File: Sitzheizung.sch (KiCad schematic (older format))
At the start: 16 parts, among them J1 Conn_01x06_Male, Q1 BUK9M9R1-40EX, U1 TL494

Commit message: started placement
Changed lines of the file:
@@
 EESchema Schematic File Version 4
+LIBS:Sitzheizung-cache
 EELAYER 26 0
 EELAYER END
@@
 Wire Wire Line
 	1250 3450 1400 3450
-$Comp
-L power:PWR_FLAG #FLG0101
-U 1 1 5B3EE6A1
-P 5750 1600
-F 0 "#FLG0101" H 5750 1675 50  0001 C CNN
-F 1 "PWR_FLAG" H 5750 1774 50  0000 C CNN
-F 2 "" H 5750 1600 50  0001 C CNN
-F 3 "~" H 5750 1600 50  0001 C CNN
-	1    5750 1600
-	1    0    0    -1
-$EndComp
 Wire Wire Line
 	5750 1600 5750 1950
@@
 	1    0    0    -1
 $EndComp
+$Comp
+L power:PWR_FLAG #FLG0103
+U 1 1 5B3D5477
+P 5050 1600
+F 0 "#FLG0103" H 5050 1675 50  0001 C CNN
+F 1 "PWR_FLAG" H 5050 1774 50  0000 C CNN
+F 2 "" H 5050 1600 50  0001 C CNN
+F 3 "~" H 5050 1600 50  0001 C CNN
+	1    5050 1600
+	1    0    0    -1
+$EndComp
+Wire Wire Line
+	5050 1600 5050 2150
+Connection ~ 5050 2150
+$Comp
+L power:PWR_FLAG #FLG0101
+U 1 1 5B3D75B4
+P 5750 1600
+F 0 "#FLG0101" H 5750 1675 50  0001 C CNN
+F 1 "PWR_FLAG" H 5750 1774 50  0000 C CNN
+F 2 "" H 5750 1600 50  0001 C CNN
+F 3 "~" H 5750 1600 50  0001 C CNN
+	1    5750 1600
+	1    0    0    -1
+$EndComp

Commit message: finished layout
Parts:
- C1, C3: footprint Capacitors_SMD:C_0805_HandSoldering -> Capacitor_SMD:C_0805_2012Metric_Pad1.15x1.40mm_HandSolder
- C2, C4: footprint Capacitors_THT:CP_Radial_D8.0mm_P5.00mm -> Capacitor_THT:CP_Radial_D8.0mm_P5.00mm
- D1: footprint Diodes_SMD:D_MiniMELF -> Diode_SMD:D_MiniMELF
- D2: footprint LEDs:LED_0805_HandSoldering -> LED_SMD:LED_0805_2012Metric_Pad0.98x1.40mm_HandSolder
- J1: footprint (none) -> Connector_TE-Connectivity:TE_MQS_936287-2_1x06_P2.54mm_Horizontal
- R1, R2, R3, R4, R5, R6: footprint Resistors_SMD:R_0805_HandSoldering -> Resistor_SMD:R_0805_2012Metric_Pad1.15x1.40mm_HandSolder
- RV1: footprint Potentiometers:Potentiometer_Trimmer_Piher_PT-10v10_Horizontal_Px10.0mm_Py5.0mm -> Potentiometer_THT:Potentiometer_Bourns_3386X_Horizontal
- U1: footprint Housings_SOIC:SOIC-16_3.9x9.9mm_Pitch1.27mm -> Package_SO:SOIC-16_3.9x9.9mm_P1.27mm
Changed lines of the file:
@@
 F 0 "U1" H 5400 4250 50  0000 C CNN
 F 1 "TL494" H 6050 3050 50  0000 C CNN
-F 2 "Housings_SOIC:SOIC-16_3.9x9.9mm_Pitch1.27mm" H 5750 3600 50  0001 C CNN
+F 2 "Package_SO:SOIC-16_3.9x9.9mm_P1.27mm" H 5750 3600 50  0001 C CNN
 F 3 "http://www.ti.com/lit/ds/symlink/tl494.pdf" H 5750 3600 50  0001 C CNN
 	1    5750 3600
@@
 F 0 "D1" H 7650 2166 50  0000 C CNN
 F 1 "D" H 7650 2075 50  0000 C CNN
-F 2 "Diodes_SMD:D_MiniMELF" H 7650 1950 50  0001 C CNN
+F 2 "Diode_SMD:D_MiniMELF" H 7650 1950 50  0001 C CNN
 F 3 "~" H 7650 1950 50  0001 C CNN
 	1    7650 1950
@@
 F 0 "R1" H 8970 2496 50  0000 L CNN
 F 1 "650R" H 8970 2405 50  0000 L CNN
-F 2 "Resistors_SMD:R_0805_HandSoldering" V 8830 2450 50  0001 C CNN
+F 2 "Resistor_SMD:R_0805_2012Metric_Pad1.15x1.40mm_HandSolder" V 8830 2450 50  0001 C CNN
 F 3 "~" H 8900 2450 50  0001 C CNN
 	1    8900 2450
@@
 F 0 "D2" V 8938 2883 50  0000 R CNN
 F 1 "LED" V 8847 2883 50  0000 R CNN
-F 2 "LEDs:LED_0805_HandSoldering" H 8900 3000 50  0001 C CNN
+F 2 "LED_SMD:LED_0805_2012Metric_Pad0.98x1.40mm_HandSolder" H 8900 3000 50  0001 C CNN
 F 3 "~" H 8900 3000 50  0001 C CNN
 	1    8900 3000
@@
 F 0 "R5" H 7970 4296 50  0000 L CNN
 F 1 "1k8" H 7970 4205 50  0000 L CNN
-F 2 "Resistors_SMD:R_0805_HandSoldering" V 7830 4250 50  0001 C CNN
+F 2 "Resistor_SMD:R_0805_2012Metric_Pad1.15x1.40mm_HandSolder" V 7830 4250 50  0001 C CNN
 F 3 "~" H 7900 4250 50  0001 C CNN
 	1    7900 4250
@@
 F 0 "R4" V 7993 3800 50  0000 C CNN
 F 1 "15k" V 8084 3800 50  0000 C CNN
-F 2 "Resistors_SMD:R_0805_HandSoldering" V 8130 3800 50  0001 C CNN
+F 2 "Resistor_SMD:R_0805_2012Metric_Pad1.15x1.40mm_HandSolder" V 8130 3800 50  0001 C CNN
 F 3 "~" H 8200 3800 50  0001 C CNN
 	1    8200 3800
@@
 F 0 "C1" H 6765 4296 50  0000 L CNN
 F 1 "100n" H 6765 4205 50  0000 L CNN
-F 2 "Capacitors_SMD:C_0805_HandSoldering" H 6688 4100 50  0001 C CNN
+F 2 "Capacitor_SMD:C_0805_2012Metric_Pad1.15x1.40mm_HandSolder" H 6688 4100 50  0001 C CNN
 F 3 "~" H 6650 4250 50  0001 C CNN
 	1    6650 4250
@@
 F 0 "C2" H 7418 4296 50  0000 L CNN
 F 1 "10u" H 7418 4205 50  0000 L CNN
-F 2 "Capacitors_THT:CP_Radial_D8.0mm_P5.00mm" H 7338 4100 50  0001 C CNN
+F 2 "Capacitor_THT:CP_Radial_D8.0mm_P5.00mm" H 7338 4100 50  0001 C CNN
 F 3 "~" H 7300 4250 50  0001 C CNN
 	1    7300 4250
@@
 F 0 "R2" H 3520 2696 50  0000 L CNN
 F 1 "R" H 3520 2605 50  0000 L CNN
-F 2 "Resistors_SMD:R_0805_HandSoldering" V 3380 2650 50  0001 C CNN
+F 2 "Resistor_SMD:R_0805_2012Metric_Pad1.15x1.40mm_HandSolder" V 3380 2650 50  0001 C CNN
 F 3 "~" H 3450 2650 50  0001 C CNN
 	1    3450 2650
@@
 F 0 "C3" H 3565 4346 50  0000 L CNN
 F 1 "100n" H 3565 4255 50  0000 L CNN
-F 2 "Capacitors_SMD:C_0805_HandSoldering" H 3488 4150 50  0001 C CNN
+F 2 "Capacitor_SMD:C_0805_2012Metric_Pad1.15x1.40mm_HandSolder" H 3488 4150 50  0001 C CNN
 F 3 "~" H 3450 4300 50  0001 C CNN
 	1    3450 4300
@@
 F 0 "RV1" H 2680 2646 50  0000 R CNN
 F 1 "15k" H 2680 2555 50  0000 R CNN
-F 2 "Potentiometers:Potentiometer_Trimmer_Piher_PT-10v10_Horizontal_Px10.0mm_Py5.0mm" H 2750 2600 50  0001 C CNN
+F 2 "Potentiometer_THT:Potentiometer_Bourns_3386X_Horizontal" H 2750 2600 50  0001 C CNN
 F 3 "~" H 2750 2600 50  0001 C CNN
 	1    2750 2600
@@
 F 0 "C4" H 5168 4346 50  0000 L CNN
 F 1 "1u" H 5168 4255 50  0000 L CNN
-F 2 "Capacitors_THT:CP_Radial_D8.0mm_P5.00mm" H 5088 4150 50  0001 C CNN
+F 2 "Capacitor_THT:CP_Radial_D8.0mm_P5.00mm" H 5088 4150 50  0001 C CNN
 F 3 "~" H 5050 4300 50  0001 C CNN
 	1    5050 4300
@@
 F 0 "R6" H 4520 4346 50  0000 L CNN
 F 1 "1k" H 4520 4255 50  0000 L CNN
-F 2 "Resistors_SMD:R_0805_HandSoldering" V 4380 4300 50  0001 C CNN
+F 2 "Resistor_SMD:R_0805_2012Metric_Pad1.15x1.40mm_HandSolder" V 4380 4300 50  0001 C CNN
 F 3 "~" H 4450 4300 50  0001 C CNN
 	1    4450 4300
@@
 F 0 "R3" V 4700 3500 50  0000 C CNN
 F 1 "1k" V 4500 3500 50  0000 C CNN
-F 2 "Resistors_SMD:R_0805_HandSoldering" V 4530 3500 50  0001 C CNN
+F 2 "Resistor_SMD:R_0805_2012Metric_Pad1.15x1.40mm_HandSolder" V 4530 3500 50  0001 C CNN
 F 3 "~" H 4600 3500 50  0001 C CNN
 	1    4600 3500
@@
 F 0 "J1" H 1150 3550 50  0000 C CNN
 F 1 "Conn_01x06_Male" H 1150 2850 50  0000 C CNN
-F 2 "" H 1050 3250 50  0001 C CNN
+F 2 "Connector_TE-Connectivity:TE_MQS_936287-2_1x06_P2.54mm_Horizontal" H 1050 3250 50  0001 C CNN
 F 3 "~" H 1050 3250 50  0001 C CNN
 	1    1050 3250

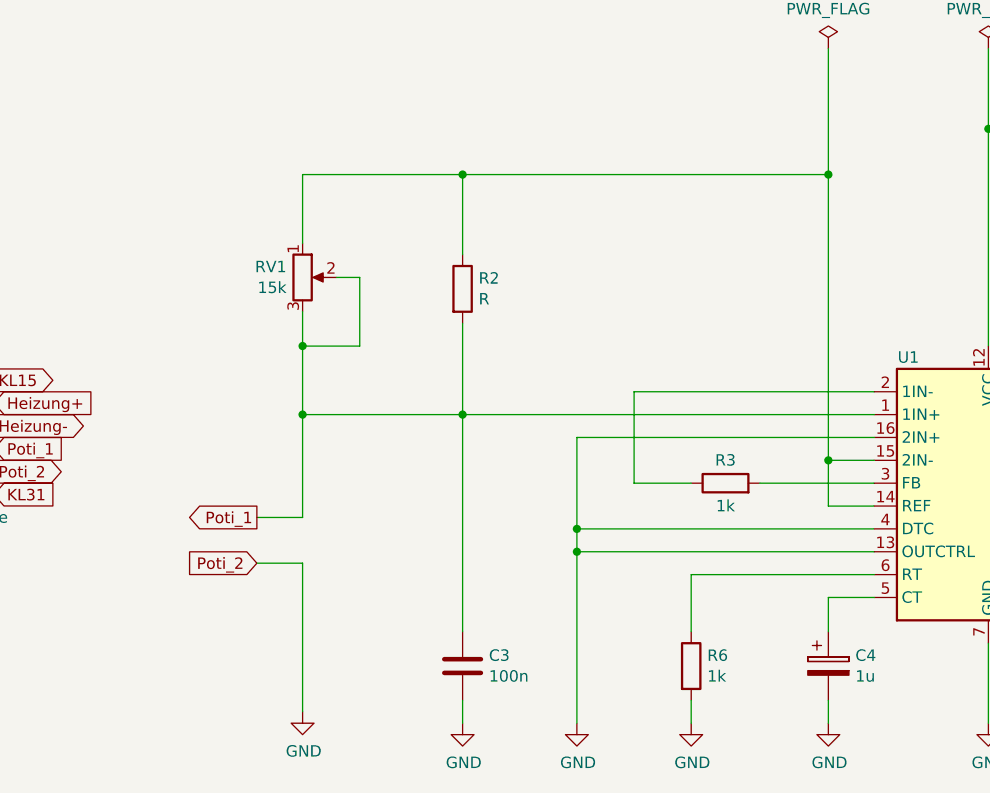
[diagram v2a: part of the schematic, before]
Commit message: changed potentiometer
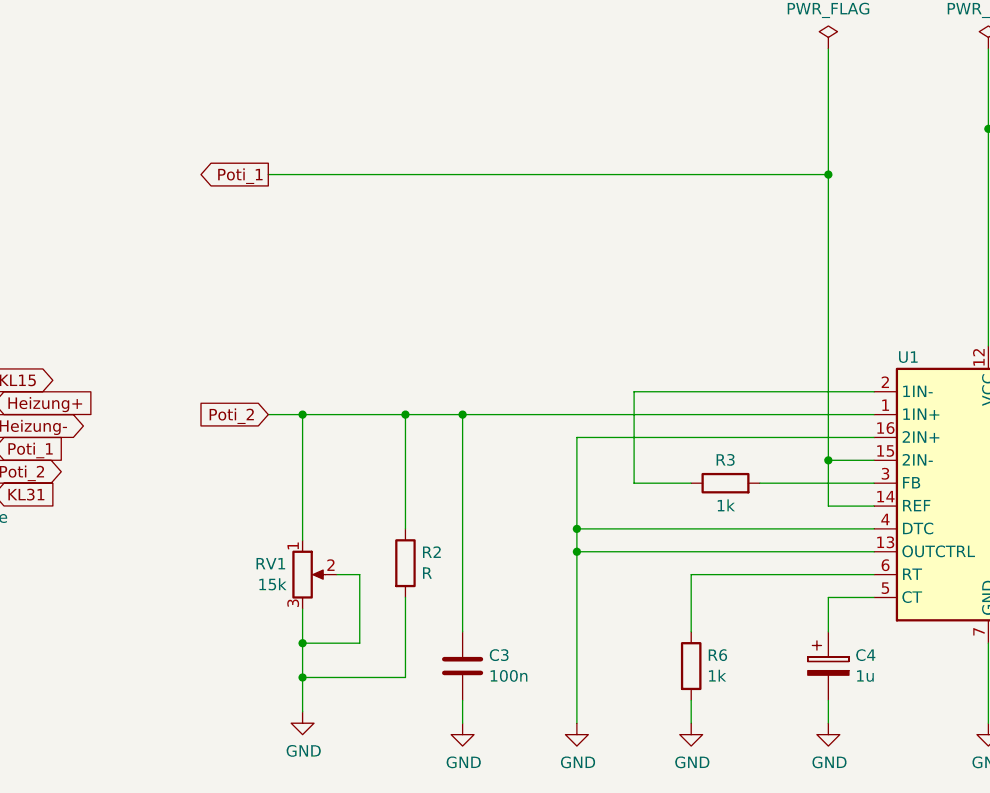
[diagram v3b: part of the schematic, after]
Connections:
- net GND: now also R2.2, RV1.2, RV1.3; no longer J1.5 (Pin_5)
- net Poti_1: now also U1.14 (REF), U1.15 (2IN-); no longer C3.1, R2.2, RV1.2, RV1.3, U1.1 (1IN+)
- net Poti_2: now reaches R2.1, RV1.1
- net Poti_2: now also C3.1, J1.5 (Pin_5), U1.1 (1IN+); no longer U1.14 (REF), U1.15 (2IN-)
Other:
- moved on the sheet: R2, RV1
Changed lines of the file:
@@
 L Device:R R2
 U 1 1 5B3BDC61
-P 3450 2650
-F 0 "R2" H 3520 2696 50  0000 L CNN
-F 1 "R" H 3520 2605 50  0000 L CNN
-F 2 "Resistor_SMD:R_0805_2012Metric_Pad1.15x1.40mm_HandSolder" V 3380 2650 50  0001 C CNN
-F 3 "~" H 3450 2650 50  0001 C CNN
-	1    3450 2650
+P 3200 3850
+F 0 "R2" H 3270 3896 50  0000 L CNN
+F 1 "R" H 3270 3805 50  0000 L CNN
+F 2 "Resistor_SMD:R_0805_2012Metric_Pad1.15x1.40mm_HandSolder" V 3130 3850 50  0001 C CNN
+F 3 "~" H 3200 3850 50  0001 C CNN
+	1    3200 3850
 	1    0    0    -1
 $EndComp
@@
 	1    0    0    -1
 $EndComp
-Wire Wire Line
-	3450 2800 3450 3200
 $Comp
 L power:GND #PWR03
@@
 Wire Wire Line
 	5050 3400 5050 2150
-Wire Wire Line
-	5050 2150 3450 2150
-Wire Wire Line
-	3450 2150 3450 2500
 Connection ~ 5050 3400
 $Comp
 L Device:R_POT RV1
 U 1 1 5B3BF5CE
-P 2750 2600
-F 0 "RV1" H 2680 2646 50  0000 R CNN
-F 1 "15k" H 2680 2555 50  0000 R CNN
-F 2 "Potentiometer_THT:Potentiometer_Bourns_3386X_Horizontal" H 2750 2600 50  0001 C CNN
-F 3 "~" H 2750 2600 50  0001 C CNN
-	1    2750 2600
-	1    0    0    -1
-$EndComp
-Wire Wire Line
-	2750 2450 2750 2150
-Wire Wire Line
-	2750 2150 3450 2150
-Connection ~ 3450 2150
-Wire Wire Line
-	2750 2750 2750 2900
-Wire Wire Line
-	2750 3650 2550 3650
-Wire Wire Line
-	2550 3850 2750 3850
+P 2750 3900
+F 0 "RV1" H 2680 3946 50  0000 R CNN
+F 1 "15k" H 2680 3855 50  0000 R CNN
+F 2 "Potentiometer_THT:Potentiometer_Bourns_3386X_Horizontal" H 2750 3900 50  0001 C CNN
+F 3 "~" H 2750 3900 50  0001 C CNN
+	1    2750 3900
+	1    0    0    -1
+$EndComp
+Wire Wire Line
+	2750 4050 2750 4200
 $Comp
 L power:GND #PWR01
@@
 	1    0    0    -1
 $EndComp
-Wire Wire Line
-	2750 3850 2750 4500
-Wire Wire Line
-	2750 3200 3450 3200
-Connection ~ 2750 3200
-Wire Wire Line
-	2750 3200 2750 3650
 Connection ~ 3450 3200
 Wire Wire Line
 	3450 3200 3450 4150
 Wire Wire Line
-	2900 2600 3000 2600
-Wire Wire Line
-	3000 2600 3000 2900
-Wire Wire Line
-	3000 2900 2750 2900
-Connection ~ 2750 2900
-Wire Wire Line
-	2750 2900 2750 3200
+	2900 3900 3000 3900
+Wire Wire Line
+	3000 3900 3000 4200
+Wire Wire Line
+	3000 4200 2750 4200
+Connection ~ 2750 4200
+Wire Wire Line
+	2750 4200 2750 4350
 Wire Wire Line
 	5250 3700 3950 3700
@@
 Text GLabel 9700 4300 2    50   Input ~ 0
 KL31
-Text GLabel 2550 3650 0    50   Output ~ 0
+Text GLabel 2600 2150 0    50   Output ~ 0
 Poti_1
-Text GLabel 2550 3850 0    50   Input ~ 0
+Text GLabel 2600 3200 0    50   Input ~ 0
 Poti_2
 Text GLabel 1400 3050 2    50   Output ~ 0
@@
 	1    0    0    -1
 $EndComp
+Wire Wire Line
+	2600 3200 2750 3200
+Wire Wire Line
+	2750 3200 2750 3750
+Connection ~ 2750 3200
+Wire Wire Line
+	2750 3200 3200 3200
+Wire Wire Line
+	2600 2150 5050 2150
+Wire Wire Line
+	3200 3700 3200 3200
+Connection ~ 3200 3200
+Wire Wire Line
+	3200 3200 3450 3200
+Wire Wire Line
+	3200 4000 3200 4350
+Wire Wire Line
+	3200 4350 2750 4350
+Connection ~ 2750 4350
+Wire Wire Line
+	2750 4350 2750 4500
 $EndSCHEMATC

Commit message: added LDO
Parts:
- added C5: 330n, Capacitor_SMD:C_0805_2012Metric_Pad1.15x1.40mm_HandSolder, symbol Device:C
- added C6: 100n, Capacitor_SMD:C_0805_2012Metric_Pad1.15x1.40mm_HandSolder, symbol Device:C
- added D?: LL4148, Diode_SMD:D_MiniMELF, symbol Device:D
- added U2: uA7805, Package_TO_SOT_SMD:SOT-223-3_TabPin2, symbol Regulator_Linear:uA7805
- C2: footprint Capacitor_THT:CP_Radial_D8.0mm_P5.00mm -> Capacitor_THT:CP_Radial_D6.3mm_P2.50mm
- C4: footprint Capacitor_THT:CP_Radial_D8.0mm_P5.00mm -> Capacitor_SMD:C_0805_2012Metric_Pad1.15x1.40mm_HandSolder; symbol Device:CP -> Device:C
- D1: value D -> LL4148
- R1: value 650R -> 1k
- RV1: value 15k -> 200R
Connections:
- net GND: now also C5.2, C6.2, U2.2 (GND)
- net Poti_1: now also C6.1, D?.2 (A), U2.3 (OUT); no longer U1.14 (REF)
- net VIN: now reaches C1.1, C2.1, D1.1 (K), U1.11 (C2), U1.12 (VCC), U1.8 (C1)
- net VIN: now also C5.1, D?.1 (K), U2.1 (IN)
- no-connect marks 0 -> 1
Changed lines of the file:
@@
 P 7650 1950
 F 0 "D1" H 7650 2166 50  0000 C CNN
-F 1 "D" H 7650 2075 50  0000 C CNN
+F 1 "LL4148" H 7650 2075 50  0000 C CNN
 F 2 "Diode_SMD:D_MiniMELF" H 7650 1950 50  0001 C CNN
 F 3 "~" H 7650 1950 50  0001 C CNN
@@
 P 8900 2450
 F 0 "R1" H 8970 2496 50  0000 L CNN
-F 1 "650R" H 8970 2405 50  0000 L CNN
+F 1 "1k" H 8970 2405 50  0000 L CNN
 F 2 "Resistor_SMD:R_0805_2012Metric_Pad1.15x1.40mm_HandSolder" V 8830 2450 50  0001 C CNN
 F 3 "~" H 8900 2450 50  0001 C CNN
@@
 F 0 "C2" H 7418 4296 50  0000 L CNN
 F 1 "10u" H 7418 4205 50  0000 L CNN
-F 2 "Capacitor_THT:CP_Radial_D8.0mm_P5.00mm" H 7338 4100 50  0001 C CNN
+F 2 "Capacitor_THT:CP_Radial_D6.3mm_P2.50mm" H 7338 4100 50  0001 C CNN
 F 3 "~" H 7300 4250 50  0001 C CNN
 	1    7300 4250
@@
 	5250 3400 5050 3400
 Wire Wire Line
-	5050 3400 5050 3600
-Wire Wire Line
-	5050 3600 5250 3600
-Wire Wire Line
 	5050 3400 5050 2150
-Connection ~ 5050 3400
 $Comp
 L Device:R_POT RV1
@@
 P 2750 3900
 F 0 "RV1" H 2680 3946 50  0000 R CNN
-F 1 "15k" H 2680 3855 50  0000 R CNN
+F 1 "200R" H 2680 3855 50  0000 R CNN
 F 2 "Potentiometer_THT:Potentiometer_Bourns_3386X_Horizontal" H 2750 3900 50  0001 C CNN
 F 3 "~" H 2750 3900 50  0001 C CNN
@@
 $EndComp
 $Comp
-L Device:CP C4
+L Device:C C4
 U 1 1 5B3C94B6
 P 5050 4300
 F 0 "C4" H 5168 4346 50  0000 L CNN
 F 1 "1u" H 5168 4255 50  0000 L CNN
-F 2 "Capacitor_THT:CP_Radial_D8.0mm_P5.00mm" H 5088 4150 50  0001 C CNN
+F 2 "Capacitor_SMD:C_0805_2012Metric_Pad1.15x1.40mm_HandSolder" H 5088 4150 50  0001 C CNN
 F 3 "~" H 5050 4300 50  0001 C CNN
 	1    5050 4300
@@
 Wire Wire Line
 	2750 4350 2750 4500
+$Comp
+L Regulator_Linear:uA7805 U2
+U 1 1 5C76FBFB
+P 8050 5250
+F 0 "U2" H 7900 5375 50  0000 C CNN
+F 1 "uA7805" H 8050 5375 50  0000 L CNN
+F 2 "Package_TO_SOT_SMD:SOT-223-3_TabPin2" H 8075 5100 50  0001 L CIN
+F 3 "http://www.ti.com/lit/ds/symlink/ua78.pdf" H 8050 5200 50  0001 C CNN
+	1    8050 5250
+	1    0    0    -1
+$EndComp
+$Comp
+L Device:C C6
+U 1 1 5C76FDD2
+P 8700 5650
+F 0 "C6" H 8815 5696 50  0000 L CNN
+F 1 "100n" H 8815 5605 50  0000 L CNN
+F 2 "Capacitor_SMD:C_0805_2012Metric_Pad1.15x1.40mm_HandSolder" H 8738 5500 50  0001 C CNN
+F 3 "~" H 8700 5650 50  0001 C CNN
+	1    8700 5650
+	1    0    0    -1
+$EndComp
+$Comp
+L power:GND #PWR0101
+U 1 1 5C76FE4A
+P 8050 5950
+F 0 "#PWR0101" H 8050 5700 50  0001 C CNN
+F 1 "GND" H 8055 5777 50  0000 C CNN
+F 2 "" H 8050 5950 50  0001 C CNN
+F 3 "" H 8050 5950 50  0001 C CNN
+	1    8050 5950
+	1    0    0    -1
+$EndComp
+Wire Wire Line
+	8050 5950 8050 5550
+Wire Wire Line
+	8350 5250 8700 5250
+Wire Wire Line
+	8700 5250 8700 5500
+$Comp
+L power:GND #PWR0102
+U 1 1 5C7740AB
+P 8700 5950
+F 0 "#PWR0102" H 8700 5700 50  0001 C CNN
+F 1 "GND" H 8705 5777 50  0000 C CNN
+F 2 "" H 8700 5950 50  0001 C CNN
+F 3 "" H 8700 5950 50  0001 C CNN
+	1    8700 5950
+	1    0    0    -1
+$EndComp
+Wire Wire Line
+	8700 5950 8700 5800
+$Comp
+L Device:C C5
+U 1 1 5C776318
+P 7300 5650
+F 0 "C5" H 7415 5696 50  0000 L CNN
+F 1 "330n" H 7415 5605 50  0000 L CNN
+F 2 "Capacitor_SMD:C_0805_2012Metric_Pad1.15x1.40mm_HandSolder" H 7338 5500 50  0001 C CNN
+F 3 "~" H 7300 5650 50  0001 C CNN
+	1    7300 5650
+	1    0    0    -1
+$EndComp
+$Comp
+L power:GND #PWR0103
+U 1 1 5C776396
+P 7300 5950
+F 0 "#PWR0103" H 7300 5700 50  0001 C CNN
+F 1 "GND" H 7305 5777 50  0000 C CNN
+F 2 "" H 7300 5950 50  0001 C CNN
+F 3 "" H 7300 5950 50  0001 C CNN
+	1    7300 5950
+	1    0    0    -1
+$EndComp
+Wire Wire Line
+	7300 5950 7300 5800
+Wire Wire Line
+	7300 5500 7300 5250
+Wire Wire Line
+	7300 5250 7750 5250
+Text Label 6950 1950 2    100  ~ 0
+VIN
+Connection ~ 8700 5250
+Text GLabel 8900 5250 2    50   Output ~ 0
+Poti_1
+Wire Wire Line
+	8900 5250 8700 5250
+NoConn ~ 5250 3600
+Text Label 7100 5250 2    100  ~ 0
+VIN
+Wire Wire Line
+	7100 5250 7300 5250
+Connection ~ 7300 5250
+$Comp
+L Device:D D?
+U 1 1 5C78511E
+P 8050 4950
+F 0 "D?" H 8050 5166 50  0000 C CNN
+F 1 "LL4148" H 8050 5075 50  0000 C CNN
+F 2 "Diode_SMD:D_MiniMELF" H 8050 4950 50  0001 C CNN
+F 3 "~" H 8050 4950 50  0001 C CNN
+	1    8050 4950
+	1    0    0    -1
+$EndComp
+Wire Wire Line
+	7900 4950 7300 4950
+Wire Wire Line
+	7300 4950 7300 5250
+Wire Wire Line
+	8200 4950 8700 4950
+Wire Wire Line
+	8700 4950 8700 5250
 $EndSCHEMATC

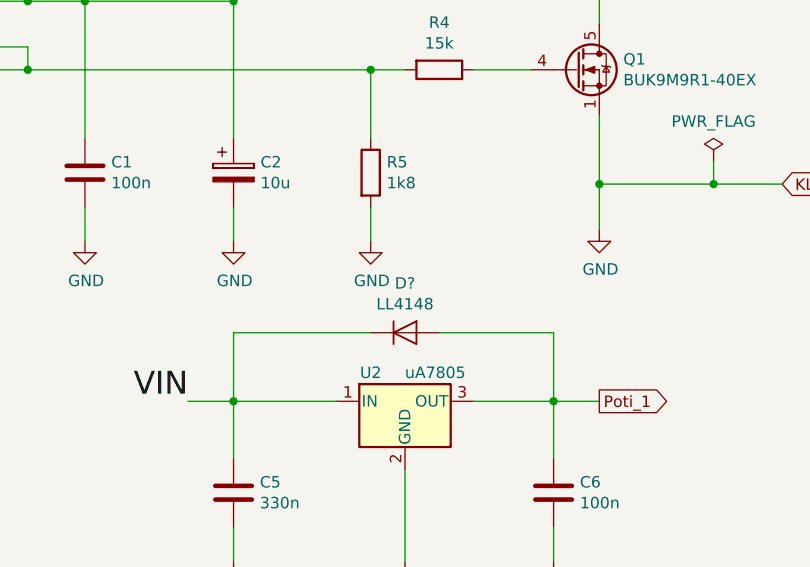
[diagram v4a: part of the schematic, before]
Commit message: missing annotation
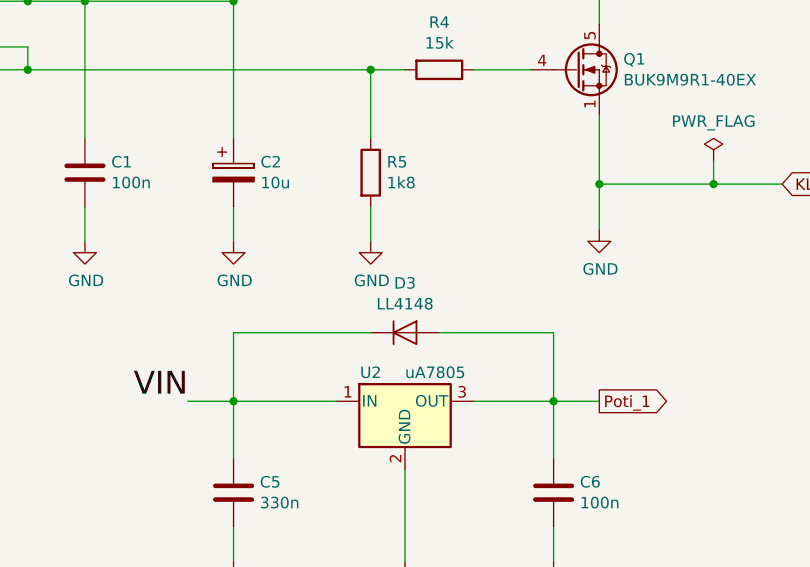
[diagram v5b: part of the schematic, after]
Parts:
- gave numbers to parts that had none: 1
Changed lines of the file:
@@
 Connection ~ 7300 5250
 $Comp
-L Device:D D?
+L Device:D D3
 U 1 1 5C78511E
 P 8050 4950
-F 0 "D?" H 8050 5166 50  0000 C CNN
+F 0 "D3" H 8050 5166 50  0000 C CNN
 F 1 "LL4148" H 8050 5075 50  0000 C CNN
 F 2 "Diode_SMD:D_MiniMELF" H 8050 4950 50  0001 C CNN
